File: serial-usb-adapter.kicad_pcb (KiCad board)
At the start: 2 copper layers, 38 x 26 mm, 29 parts, among them J1 USB_B_Mini, J2 UART Header, U1 LPC47M192, U2 FT231XS, Y1 SG5032CAN 14.318MHz

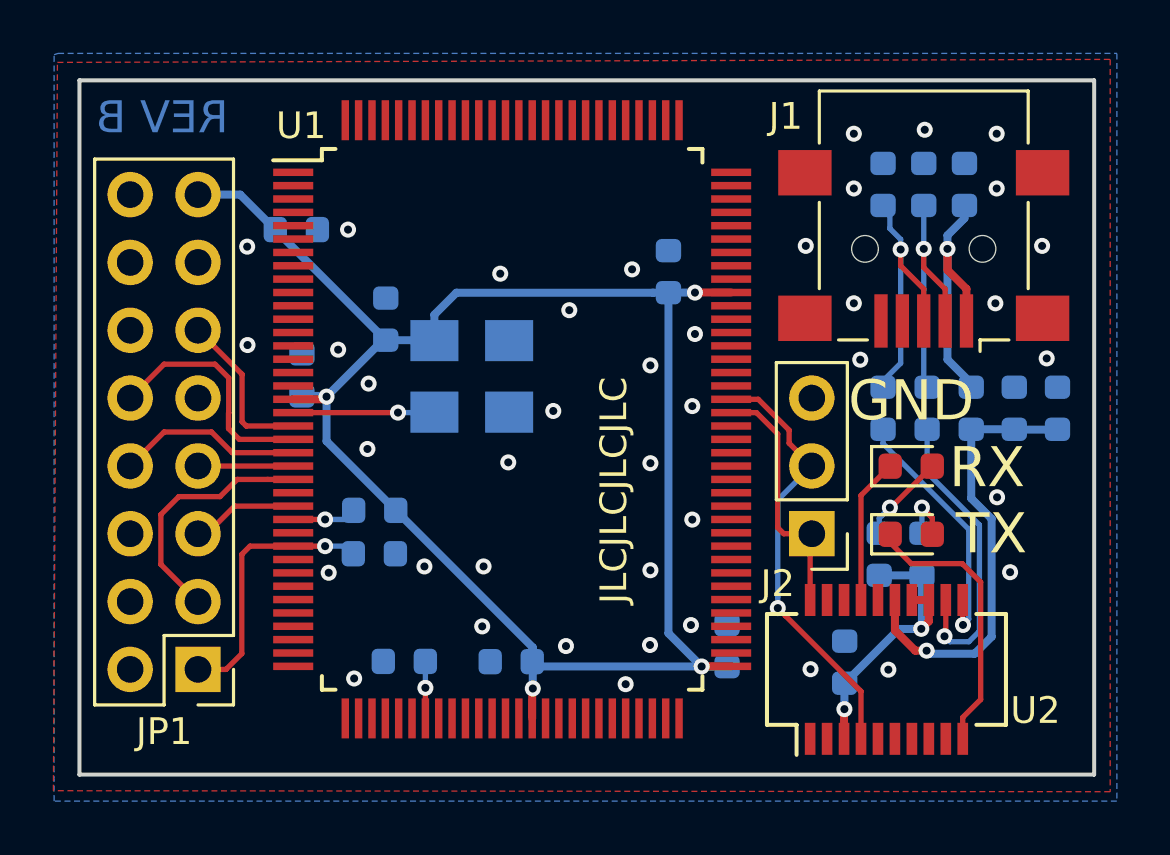
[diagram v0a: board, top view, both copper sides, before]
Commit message: Replace Mini USB connector with Micro USB
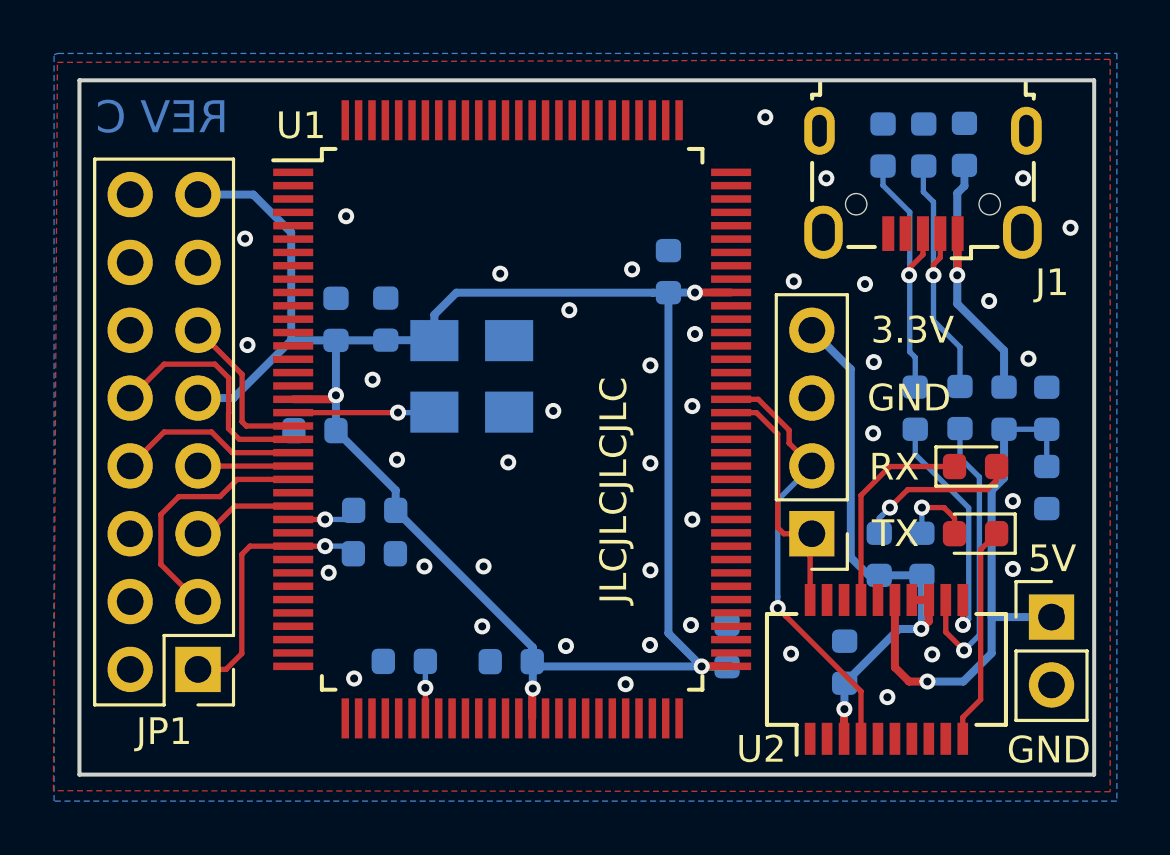
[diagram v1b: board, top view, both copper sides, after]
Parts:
- added J3: USB Power, Connector_PinHeader_2.54mm:PinHeader_1x02_P2.54mm_Vertical, F.Cu at (129.2, 127.6)
- J1: value USB_B_Mini -> USB_B_Micro; footprint Connector_USB:USB_Mini-B_Lumberg_2486_01_Horizontal -> Connector_USB:USB_Micro-B_Wuerth_629105150521
- J2: footprint Connector_PinHeader_2.54mm:PinHeader_1x03_P2.54mm_Vertical -> Connector_PinHeader_2.54mm:PinHeader_1x04_P2.54mm_Vertical
- moved OSHW Logo 15.3 mm to (114.4, 121.8)
- moved C5 3.67 mm to (102.4, 116.4), turned to -90 degrees
- moved C1 3.00 mm to (129.0, 122.7), turned to -90 degrees
- moved J1 2.47 mm to (124.4, 111.3)
- moved D2 2.41 mm to (126.4, 121.9)
- moved D1 2.41 mm to (126.4, 124.4), turned to 180 degrees
- moved C8 2.14 mm to (101.6, 120.6), turned to 180 degrees
- moved C3 1.50 mm to (125.9, 109.9)
- moved C6 1.48 mm to (122.9, 109.9)
- moved C7 1.48 mm to (124.4, 109.9)
- moved R3 1.23 mm to (125.8, 119.7)
- moved FB1 1.23 mm to (127.4, 119.7)
- moved C2 1.22 mm to (129.0, 119.7)
- moved R1 1.20 mm to (124.1, 119.7)
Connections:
- J1 pad 4: VSS -> unconnected-(J1-Pad4)
- JP1 pad 9: (no net) -> VCC
- Y1 pad 1: Net-(Y1-Pad1) -> unconnected-(Y1-Pad1)
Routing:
- net +3V3: track 11.3 -> 21.8 mm
- net VCC: track 67.2 -> 72.3 mm
- net VBUS: track 16.7 -> 20.6 mm, vias 1 -> 2
- net Net-(D2-Pad2): track 3.36 -> 6.10 mm
- net Net-(D2-Pad1): track 5.46 -> 7.87 mm
- net Net-(D1-Pad1): track 10.5 -> 8.21 mm
- net Net-(D1-Pad2): track 2.12 -> 2.93 mm
- net Net-(C7-Pad1): track 9.89 -> 10.5 mm
- net Net-(R1-Pad1): track 9.71 -> 9.19 mm
- net VSS: track 0.14 -> 0.00 mm, vias 41 -> 40
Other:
- net class Default removed
- board text added: "3.3V"
- board text added: "5V"
- board text added: "REV C"
- board text removed: "REV B"

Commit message: Adds USB-C based Xbox Serial USB Adapter (Rev D)
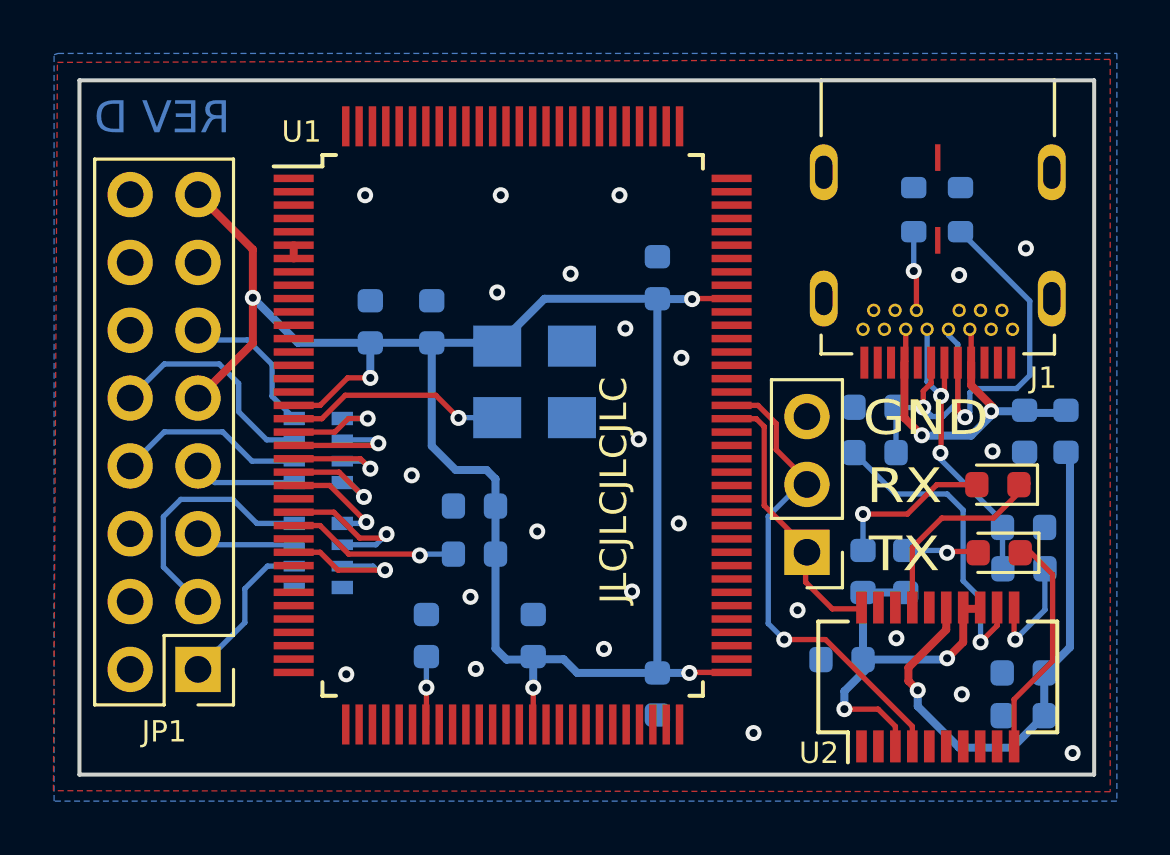
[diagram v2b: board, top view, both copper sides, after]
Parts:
- removed C4: 47pF, Capacitor_SMD:C_0603_1608Metric
- removed J3: USB Power, Connector_PinHeader_2.54mm:PinHeader_1x02_P2.54mm_Vertical
- removed OSHW Logo: OSHW-Symbol_6.7x6mm_SilkScreen, Symbol:OSHW-Symbol_6.7x6mm_SilkScreen
- added R7: 5.1k, Resistor_SMD:R_0603_1608Metric, B.Cu at (124.0, 112.3)
- added R8: 5.1k, Resistor_SMD:R_0603_1608Metric, B.Cu at (125.8, 112.3)
- added REF**: OSHW-Symbol_6.7x6mm_SilkScreen, Symbol:OSHW-Symbol_6.7x6mm_SilkScreen, B.Cu at (115.2, 122.0)
- added RN1: 100R, Resistor_SMD:R_Array_Convex_4x0603, B.Cu at (101.8, 121.3)
- added RN2: 100R, Resistor_SMD:R_Array_Convex_4x0603, B.Cu at (101.8, 125.2)
- J1: value USB_B_Micro -> USB-C; footprint Connector_USB:USB_Micro-B_Wuerth_629105150521 -> Library:SS-52400-003
- moved C6 15.3 mm to (128.2, 124.2), turned to 0 degrees
- moved C2 11.5 mm to (128.2, 131.2), turned to 180 degrees
- moved C3 11.0 mm to (128.2, 120.6), turned to -90 degrees
- moved C7 9.99 mm to (122.6, 119.7), turned to 180 degrees
- moved C5 8.71 mm to (107.6, 123.4), turned to 0 degrees
- moved R1 7.26 mm to (128.2, 125.8), turned to 180 degrees
- moved C1 7.00 mm to (128.2, 129.7), turned to 180 degrees
- moved C8 4.57 mm to (103.7, 116.5), turned to 90 degrees
- moved R2 4.08 mm to (107.6, 125.2)
- moved R3 3.60 mm to (122.6, 121.4), turned to 180 degrees
- moved C10 3.17 mm to (114.5, 130.4), turned to -90 degrees
- moved FB1 2.47 mm to (129.8, 120.6)
- moved Y1 2.36 mm to (109.8, 118.8)
- moved U2 1.94 mm to (125.0, 129.8)
- moved C13 1.73 mm to (106.0, 116.5)
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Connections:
- JP1 pad 1: Net-(C4-Pad1) -> Net-(JP1-Pad1)
- U1 pad 20: Net-(JP1-Pad11) -> Net-(RN1-Pad1)
- U1 pad 21: Net-(JP1-Pad10) -> Net-(RN1-Pad2)
- U1 pad 22: Net-(JP1-Pad8) -> Net-(RN1-Pad3)
- U1 pad 23: Net-(JP1-Pad7) -> Net-(RN1-Pad4)
- U1 pad 24: Net-(JP1-Pad3) -> Net-(RN2-Pad1)
- U1 pad 26: Net-(JP1-Pad5) -> Net-(RN2-Pad2)
- U1 pad 29: Net-(C4-Pad1) -> Net-(RN2-Pad3)
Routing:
- net Net-(J1-PadA5): track 0.00 -> 12.1 mm, vias 0 -> 1
- net Net-(C4-Pad1): track 10.0 -> 0.00 mm, vias 1 -> 0
- net +3V3: track 21.8 -> 15.2 mm
- net Net-(JP1-Pad1): track 0.00 -> 5.95 mm
- net Net-(RN2-Pad2): track 0.00 -> 5.76 mm, vias 0 -> 1
- net Net-(RN2-Pad3): track 0.00 -> 5.36 mm, vias 0 -> 1
- net Net-(R1-Pad1): track 9.19 -> 4.28 mm
- net Net-(RN1-Pad2): track 0.00 -> 4.61 mm, vias 0 -> 1
- net Net-(RN2-Pad1): track 0.00 -> 4.21 mm, vias 0 -> 1
- net Net-(RN1-Pad3): track 0.00 -> 4.19 mm, vias 0 -> 1
- net Net-(RN1-Pad4): track 0.00 -> 4.05 mm, vias 0 -> 1
- net Net-(R2-Pad1): track 2.48 -> 6.47 mm
- net Net-(RN1-Pad1): track 0.00 -> 3.93 mm, vias 0 -> 1
- net Net-(U1-Pad19): track 5.29 -> 8.34 mm
- net Net-(J1-PadB5): track 0.00 -> 2.99 mm, vias 0 -> 1
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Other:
- board text added: "REV D"
- board text removed: "3.3V"
- board text removed: "5V"
- board text removed: "REV C"
